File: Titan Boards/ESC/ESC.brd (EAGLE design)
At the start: 101.6 x 101.6 mm, 113 parts, among them Q1 2N2222, Q10 BSS138, Q3 BSS138, Q4 BSS138, Q5 BSS138, Q6 BSS138, Q7 BSS138, Q8 BSS138, Q9 BSS138

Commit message: ESC work
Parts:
- moved CS_7 83.5 mm to (33.3, 21.1)
- moved C7 83.5 mm to (29.7, 21.1)
- moved D9 83.5 mm to (26.9, 24.6)
- moved FUSE_7 83.5 mm to (30.2, 27.9)
- moved Q9 83.5 mm to (20.8, 25.7)
- moved R20 83.5 mm to (27.4, 22.4)
- moved R21 83.5 mm to (23.6, 29.0)
- moved R22 83.5 mm to (23.6, 25.7)
- moved C3 81.5 mm to (65.8, 21.1)
- moved CS_5 81.5 mm to (69.3, 21.1)
- moved D7 81.5 mm to (63.0, 24.6)
- moved FUSE_5 81.5 mm to (66.3, 27.9)
- moved Q7 81.5 mm to (57.1, 25.7)
- moved R14 81.5 mm to (63.5, 22.4)
- moved R15 81.5 mm to (59.7, 29.0)
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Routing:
- net FAULT_8: track 6.49 -> 92.2 mm
- net ANALOG_8: track 0.00 -> 73.9 mm, vias 0 -> 1
- net ANALOG_7: track 0.00 -> 54.1 mm, vias 0 -> 1
- net ANALOG_6: track 0.00 -> 34.6 mm, vias 0 -> 1
- net FUSE_2_TRIGGER: track 4.69 -> 28.7 mm, vias 0 -> 1
- net FUSE_1_TRIGGER: track 5.05 -> 28.6 mm, vias 0 -> 1
- net FUSE_3_TRIGGER: track 4.43 -> 27.6 mm, vias 0 -> 1
- net FUSE_4_TRIGGER: track 4.99 -> 28.2 mm, vias 0 -> 1
- net FUSE_8_TRIGGER: track 4.19 -> 14.0 mm
- net FUSE_6_TRIGGER: track 4.19 -> 14.0 mm
- net FUSE_5_TRIGGER: track 4.19 -> 13.6 mm
- net FUSE_7_TRIGGER: track 4.42 -> 13.8 mm
- net ANALOG_5: track 0.00 -> 6.45 mm, vias 0 -> 1
- net FAULT_7: track 6.74 -> 2.32 mm

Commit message: more esc work
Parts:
- moved Q1 94.1 mm to (4.78, 50.0)
- moved D2 94.1 mm to (9.35, 50.5)
- moved R28 94.1 mm to (9.60, 48.7)
- moved R37 94.1 mm to (9.60, 52.3)
- moved R29 86.7 mm to (2.48, 45.6), turned to 0 degrees
- moved R33 86.7 mm to (2.48, 45.6), turned to 180 degrees
- moved R32 74.7 mm to (2.48, 43.3), turned to 180 degrees
- moved R34 74.7 mm to (2.48, 43.3), turned to 0 degrees
- moved R31 65.5 mm to (2.48, 40.9), turned to 180 degrees
- moved R35 65.5 mm to (2.48, 40.9), turned to 0 degrees
- moved R30 60.4 mm to (2.48, 38.5), turned to 180 degrees
- moved R36 60.4 mm to (2.48, 38.5), turned to 0 degrees
- moved 3-PIN_5 2.10 mm to (66.0, 79.9)
- moved 3-PIN_6 2.10 mm to (48.3, 79.9)
- moved 3-PIN_7 2.10 mm to (30.5, 79.9)
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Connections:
- removed net N$1 (its old number): 24-PIN_CONNECTOR.7,WHITE, 3-PIN_1.WHITE
- removed net N$13: 24-PIN_CONNECTOR.8,WHITE, 3-PIN_5.WHITE
- removed net N$14: 24-PIN_CONNECTOR.8,GREEN, 3-PIN_5.GREEN
- removed net N$15: 24-PIN_CONNECTOR.8,BLUE, 3-PIN_5.BLUE
- removed net N$16: 24-PIN_CONNECTOR.6,WHITE, 3-PIN_6.WHITE
- removed net N$17: 24-PIN_CONNECTOR.6,GREEN, 3-PIN_6.GREEN
- removed net N$18: 24-PIN_CONNECTOR.6,BLUE, 3-PIN_6.BLUE
- removed net N$19: 24-PIN_CONNECTOR.4,WHITE, 3-PIN_7.WHITE
- removed net N$2 (its old number): 24-PIN_CONNECTOR.7,GREEN, 3-PIN_1.GREEN
- removed net N$20: 24-PIN_CONNECTOR.4,BLUE, 3-PIN_7.BLUE
- removed net N$21: 24-PIN_CONNECTOR.4,GREEN, 3-PIN_7.GREEN
- removed net N$22: 24-PIN_CONNECTOR.2,BLUE, 3-PIN_8.BLUE
- removed net N$23: 24-PIN_CONNECTOR.2,GREEN, 3-PIN_8.GREEN
- removed net N$24: 24-PIN_CONNECTOR.2,WHITE, 3-PIN_8.WHITE
- removed net N$3 (its old number): 24-PIN_CONNECTOR.7,BLUE, 3-PIN_1.BLUE
- removed net N$4 (its old number): 24-PIN_CONNECTOR.5,WHITE, 3-PIN_2.WHITE
- removed net N$5 (its old number): 24-PIN_CONNECTOR.5,GREEN, 3-PIN_2.GREEN
- removed net N$6 (its old number): 24-PIN_CONNECTOR.5,BLUE, 3-PIN_2.BLUE
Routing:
- net N$1: track 0.00 -> 146.1 mm
- net N$40: track 133.4 -> 2.11 mm
- net N$2: track 0.00 -> 130.5 mm
- net PWM_4: track 0.00 -> 127.1 mm
- net PWM_8: track 0.00 -> 121.1 mm, vias 0 -> 2
- net N$6: track 0.00 -> 119.4 mm
- net N$3: track 0.00 -> 114.6 mm
- net PWM_3: track 0.00 -> 110.9 mm
- net N$5: track 0.00 -> 105.0 mm
- net PWM_7: track 0.00 -> 104.3 mm, vias 0 -> 2
- net PWM_2: track 0.00 -> 92.4 mm
- net N$4: track 0.00 -> 89.8 mm
- net PWM_6: track 0.00 -> 86.0 mm, vias 0 -> 2
- net FAULT_1: track 7.46 -> 93.4 mm
- net FAULT_8: track 92.2 -> 6.49 mm
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
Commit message: Titan ESC updates
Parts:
- moved Q1 18.6 mm to (-7.02, 35.6)
- moved D2 18.6 mm to (-2.45, 36.1)
- moved R28 18.6 mm to (-2.20, 34.3)
- moved R37 18.6 mm to (-2.20, 37.9)
- moved R36 7.75 mm to (-5.12, 40.0)
- moved R30 7.73 mm to (-5.12, 39.9)
- moved R29 7.73 mm to (-5.12, 47.0)
- moved R31 7.73 mm to (-5.12, 42.3)
- moved R32 7.73 mm to (-5.12, 44.7)
- moved R33 7.73 mm to (-5.12, 47.0)
- moved R35 7.71 mm to (-5.12, 42.2)
- moved R34 7.68 mm to (-5.12, 44.4)
- moved THRUSTER_PWM_1 6.40 mm to (76.0, 38.0)
- moved THRUSTER_PWM_2 6.40 mm to (58.2, 38.0)
- moved THRUSTER_PWM_3 6.40 mm to (40.4, 38.0)
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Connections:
- new net N$10: 24-PIN_CONNECTOR.7,BLUE, 3-PIN_1.BLUE
- new net N$11: 24-PIN_CONNECTOR.7,GREEN, 3-PIN_1.GREEN
- new net N$12: 24-PIN_CONNECTOR.7,WHITE, 3-PIN_1.WHITE
- new net N$13: 24-PIN_CONNECTOR.8,BLUE, 3-PIN_5.WHITE
- new net N$14: 24-PIN_CONNECTOR.8,GREEN, 3-PIN_5.GREEN
- new net N$15: 24-PIN_CONNECTOR.8,WHITE, 3-PIN_5.BLUE
- new net N$16: 24-PIN_CONNECTOR.6,WHITE, 3-PIN_6.WHITE
- new net N$17: 24-PIN_CONNECTOR.6,GREEN, 3-PIN_6.GREEN
- new net N$18: 24-PIN_CONNECTOR.6,BLUE, 3-PIN_6.BLUE
- new net N$19: 24-PIN_CONNECTOR.4,BLUE, 3-PIN_7.BLUE
- new net N$20: 24-PIN_CONNECTOR.4,GREEN, 3-PIN_7.GREEN
- new net N$21: 24-PIN_CONNECTOR.4,WHITE, 3-PIN_7.WHITE
- new net N$22: 24-PIN_CONNECTOR.2,BLUE, 3-PIN_8.BLUE
- new net N$23: 24-PIN_CONNECTOR.2,GREEN, 3-PIN_8.GREEN
- new net N$24: 24-PIN_CONNECTOR.2,WHITE, 3-PIN_8.WHITE
- new net N$7: 24-PIN_CONNECTOR.5,BLUE, 3-PIN_2.BLUE
- new net N$8: 24-PIN_CONNECTOR.5,GREEN, 3-PIN_2.GREEN
- new net N$9: 24-PIN_CONNECTOR.5,WHITE, 3-PIN_2.WHITE
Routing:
- net N$24: track 0.00 -> 85.9 mm
- net N$7: track 0.00 -> 82.7 mm
- net N$5: track 105.0 -> 186.9 mm
- net N$23: track 0.00 -> 79.6 mm
- net N$22: track 0.00 -> 73.2 mm
- net N$8: track 0.00 -> 69.7 mm
- net N$21: track 0.00 -> 65.3 mm
- net N$20: track 0.00 -> 59.0 mm
- net N$9: track 0.00 -> 58.7 mm
- net N$19: track 0.00 -> 52.7 mm
- net N$16: track 0.00 -> 45.2 mm
- net N$10: track 0.00 -> 45.0 mm
- net N$6: track 119.4 -> 162.0 mm
- net N$1: track 146.1 -> 107.0 mm
- net N$17: track 0.00 -> 38.9 mm
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
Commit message: more changes to ESC board
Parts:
- removed Q10, Q9: BSS138, SparkFun-DiscreteSemi:SOT23-3
- removed R29, R30, R31, R32, R33, R34, R35, R36: 2k, rcl:R0603
- removed R37: 4.7K, rcl:R0603
- added IC1: 7425D, 74xx-us:SO14
- added IC2: 74AHC1G08DBV, 74xx-little-us:SOT23-5
- added Q2: 5.8A/30V/35mΩ, SparkFun-DiscreteSemi:SOT23-3
- D10, D3, D4, D5, D6, D7, D8, D9: value RED -> Red
- Q1: value 2N2222 -> 5.8A/30V/35mΩ
- Q3, Q4, Q5, Q6, Q7, Q8: value BSS138 -> 5.8A/30V/35mΩ
- R10, R13, R16, R4, R7: value 190 -> (none)
- R11, R14, R17, R2, R20, R23, R5, R8: value 128 -> (none)
- R12, R15, R18, R6, R9: value 2.2K -> 28
- R19, R22, R25: value 190 -> 28
- R21, R24, R3: value 2.2K -> (none)
- moved D2 116.7 mm to (99.0, 93.8), turned to 135 degrees
- moved Q1 85.3 mm to (76.2, 16.9)
- moved R13 60.4 mm to (79.5, 17.7), flipped to the bottom, turned to 180 degrees
- moved Q4 41.3 mm to (16.2, 16.7)
- moved Q3 39.7 mm to (36.4, 16.8)
- moved R18 38.8 mm to (79.5, 16.4), flipped to the top, turned to 180 degrees
- moved Q5 36.9 mm to (76.2, 16.9), flipped to the bottom
- moved Q6 34.9 mm to (56.4, 16.7), flipped to the bottom
- moved R10 24.2 mm to (12.7, 17.8), turned to 180 degrees
- moved Q8 22.6 mm to (16.2, 16.7)
- moved CS_1 22.5 mm to (84.5, 21.1)
- moved R7 22.2 mm to (32.8, 17.5), turned to 180 degrees
- moved CS_2 20.8 mm to (64.5, 21.2)
- moved R4 20.7 mm to (52.8, 17.8), turned to 180 degrees
- moved Q7 20.7 mm to (36.4, 16.8)
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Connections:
- removed net N$54: D10.A, R23.1
- removed net N$59: D2.C, R28.1
- new net N$32: D3.C, Q1.3
- new net NOR_1_OUT: IC1.6, IC2.1
- new net NOR_2_OUT: IC1.8, IC2.2
- net +5V: now also IC1.11, IC1.14, IC1.3, IC2.5, R12.2, R15.2, R18.2, R19.2, R22.2, R25.2, R6.2, R9.2; no longer Q1.3, R11.2, R14.2, R17.2, R2.2, R20.2, R23.2, R5.2, R8.2
- net FAULT_1: now also IC1.1, Q1.1, R2.1, R3.2; no longer D3.C, Q3.3, R33.1
- net FAULT_2: now also IC1.2, Q2.1, R4.1, R5.2; no longer D4.C, Q4.3, R32.1
- net FAULT_3: now also IC1.4, Q3.1, R7.1, R8.2; no longer D5.C, Q5.3, R31.1
- net FAULT_4: now also IC1.5, Q4.1, R10.1, R11.2; no longer D6.C, Q6.3, R30.1
- net FAULT_5: now also IC1.9, Q5.1, R13.1, R14.2; no longer D7.C, Q7.3, R29.1
- net FAULT_6: now also IC1.10, Q6.1, R16.1, R17.2; no longer D8.C, Q8.3, R34.1
- net FAULT_7: now also IC1.12, Q7.1, R20.1, R21.2; no longer D9.C, Q9.3, R35.1
- net FAULT_8: now also IC1.13, Q8.1, R23.1, R24.2; no longer D10.C, Q10.3, R36.1
- net FUSE_1_TRIGGER: now also R2.2; no longer R3.2
- net FUSE_2_TRIGGER: now also R4.2; no longer R6.2
- net FUSE_3_TRIGGER: now also R7.2; no longer R9.2
- net FUSE_4_TRIGGER: now also R10.2; no longer R12.2
- net FUSE_5_TRIGGER: now also R13.2; no longer R15.2
- net FUSE_6_TRIGGER: now also R16.2; no longer R18.2
- net FUSE_7_TRIGGER: now also R20.2; no longer R21.2
- net FUSE_8_TRIGGER: now also R23.2; no longer R24.2
- net GND: now also D2.C, IC1.7, IC2.3, Q1.2, Q2.2, R11.1, R14.1, R17.1, R21.1, R24.1, R3.1, R5.1, R8.1; no longer Q10.2, Q9.2, R10.1, R13.1, R16.1, R19.1, R22.1, R25.1, R28.2, R37.2, R4.1, R7.1
- net N$13: now also 24-PIN_CONNECTOR.8,WHITE; no longer 24-PIN_CONNECTOR.8,BLUE
- net N$15: now also 24-PIN_CONNECTOR.8,BLUE; no longer 24-PIN_CONNECTOR.8,WHITE
- net N$31: now also IC2.4, R28.2; no longer D3.A, R2.1
- net N$33: now also D3.A, R18.1; no longer D4.A, R5.1
- net N$34: now also D4.C, Q2.3; no longer Q3.1, R3.1, R4.2
- net N$36: now also D4.A; no longer Q4.1, R7.2
- net N$37: now also D5.C, Q3.3; no longer D5.A, R8.1
- net N$40: now also D5.A, R9.1; no longer Q1.1, R29.2, R30.2, R31.2, R32.2, R33.2, R34.2, R35.2, R36.2
- net N$41: now also D6.C, Q4.3; no longer Q5.1, R10.2, R9.1
- net N$42: now also R12.1; no longer R11.1
- net N$44: now also D7.C, Q5.3; no longer Q6.1, R12.1, R13.2
- net N$45: now also R15.1; no longer R14.1
- net N$46: now also D8.C, Q6.3; no longer D2.A, Q1.2, R37.1
- net N$47: now also D8.A, R19.1; no longer Q7.1, R15.1, R16.2
- net N$48: now also D9.C, Q7.3; no longer D8.A, R17.1
- net N$50: now also D9.A, R22.1; no longer Q8.1, R18.1, R19.2
- net N$51: now also D10.C, Q8.3; no longer D9.A, R20.1
- net N$53: now also D10.A, R25.1; no longer Q9.1, R21.1, R22.2
- net N$56: now also D2.A, R28.1; no longer Q10.1, R24.1, R25.2
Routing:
- net N$56: track 3.18 -> 137.9 mm
- net N$4: track 94.5 -> 191.9 mm
- net FAULT_1: track 93.4 -> 2.91 mm
- net FAULT_2: track 73.0 -> 3.05 mm
- net FAULT_5: track 68.0 -> 2.77 mm, vias 2 -> 0
- net +5V: track 53.9 -> 0.00 mm
- net FAULT_3: track 53.6 -> 3.16 mm
- net FAULT_6: track 49.1 -> 2.89 mm, vias 2 -> 0
- net PWM_5: track 45.1 -> 80.6 mm
- net FAULT_4: track 32.4 -> 3.10 mm, vias 2 -> 0
- net FAULT_7: track 29.1 -> 3.12 mm, vias 2 -> 0
- net PWM_8: track 114.3 -> 137.9 mm
- net PWM_7: track 96.8 -> 118.6 mm, vias 0 -> 2
- net ANALOG_8: track 71.9 -> 92.4 mm
- net PWM_6: track 79.9 -> 99.8 mm
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- removed copper zone on layer 1, net +3V3
- removed copper zone on layer 16, net +3V3
- removed copper zone on layer 1, net +5V
- removed copper zone on layer 16, net +5V
- removed copper zone on layer 16, net GND
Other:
- outline, holes or cut-outs redrawn

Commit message: ESC board updates
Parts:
- removed THRUSTER_PWM_1: 1, pinhead:1X03
- removed THRUSTER_PWM_2, THRUSTER_PWM_3, THRUSTER_PWM_4, THRUSTER_PWM_5, THRUSTER_PWM_6, THRUSTER_PWM_7, THRUSTER_PWM_8: (no value), pinhead:1X03
- added U$1, U$2, U$3, U$4, U$5, U$6, U$7, U$8: MALE1PINHEADER, Male_Header_1Pin:MALE1PINHEADER
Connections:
- net GND: no longer THRUSTER_PWM_1.3, THRUSTER_PWM_2.3, THRUSTER_PWM_3.3, THRUSTER_PWM_4.3, THRUSTER_PWM_5.3, THRUSTER_PWM_6.3, THRUSTER_PWM_7.3, THRUSTER_PWM_8.3
- net PWM_1: now also U$1.PWM; no longer THRUSTER_PWM_1.1
- net PWM_2: now also U$2.PWM; no longer THRUSTER_PWM_2.1
- net PWM_3: now also U$3.PWM; no longer THRUSTER_PWM_3.1
- net PWM_4: now also U$4.PWM; no longer THRUSTER_PWM_4.1
- net PWM_5: now also U$5.PWM; no longer THRUSTER_PWM_5.1
- net PWM_6: now also U$6.PWM; no longer THRUSTER_PWM_6.1
- net PWM_7: now also U$7.PWM; no longer THRUSTER_PWM_7.1
- net PWM_8: now also U$8.PWM; no longer THRUSTER_PWM_8.1
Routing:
- net PWM_8: track 137.9 -> 13.4 mm
- net PWM_4: track 125.4 -> 14.1 mm
- net FAULT_5: track 2.77 -> 111.6 mm, vias 0 -> 3
- net FAULT_1: track 2.91 -> 110.0 mm, vias 0 -> 2
- net PWM_7: track 118.6 -> 13.4 mm, vias 2 -> 0
- net PWM_3: track 107.0 -> 14.3 mm
- net FAULT_6: track 2.89 -> 90.8 mm, vias 0 -> 3
- net PWM_6: track 99.8 -> 13.6 mm, vias 2 -> 0
- net FAULT_2: track 3.05 -> 88.1 mm, vias 0 -> 2
- net PWM_2: track 88.5 -> 14.3 mm
- net FAULT_7: track 3.12 -> 72.1 mm, vias 0 -> 3
- net PWM_5: track 80.6 -> 13.8 mm, vias 2 -> 0
- net FAULT_3: track 3.16 -> 61.7 mm, vias 0 -> 4
- net FAULT_8: track 3.31 -> 48.7 mm, vias 0 -> 1
- net FAULT_4: track 3.10 -> 40.0 mm
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- added copper zone on layer 16, net GND

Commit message: FInal ESC after review
See summary
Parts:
- moved 3-PIN_6 0.15 mm to (56.3, 86.5)
- moved 3-PIN_7 0.15 mm to (36.3, 86.5)
- moved 3-PIN_5 0.11 mm to (76.1, 86.5)
- moved C10 0.07 mm to (89.3, 12.7)
- renumbered FUSE_1 to F1, FUSE_2 to F2, FUSE_3 to F3, FUSE_4 to F4, FUSE_5 to F5, FUSE_6 to F6, FUSE_7 to F7, FUSE_8 to F8
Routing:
- net +5V: track 0.00 -> 222.5 mm, vias 0 -> 24
- net +3V3: track 3.71 -> 97.0 mm, vias 0 -> 4
- net GND: track 5.34 -> 92.4 mm, vias 14 -> 37
- net NOR_1_OUT: track 17.2 -> 20.2 mm
- added copper zone on layer 1, net +3V3
- added copper zone on layer 16, net +3V3
- added copper zone on layer 1, net +5V
- added copper zone on layer 16, net +5V

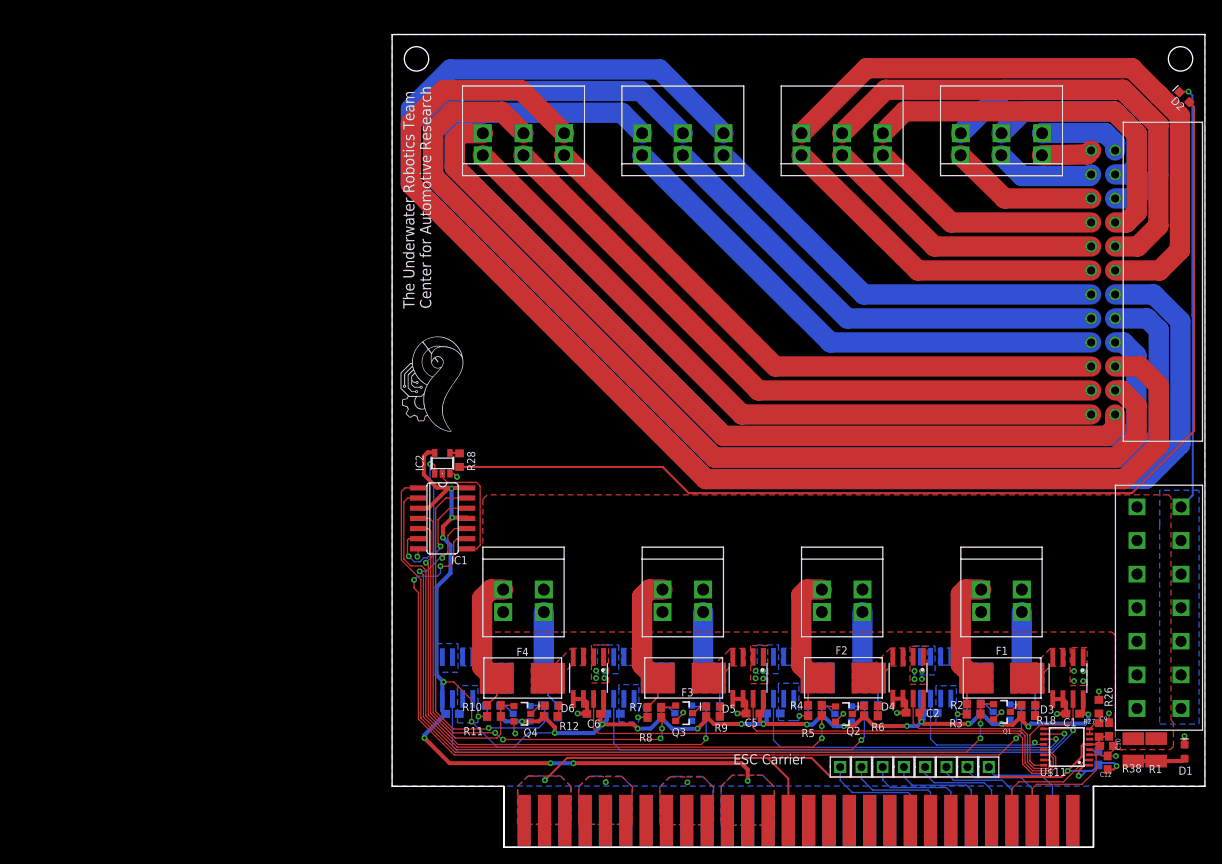
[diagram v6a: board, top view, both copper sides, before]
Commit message: final commit of Titan ESC
slight cosmetic changes to ESC board
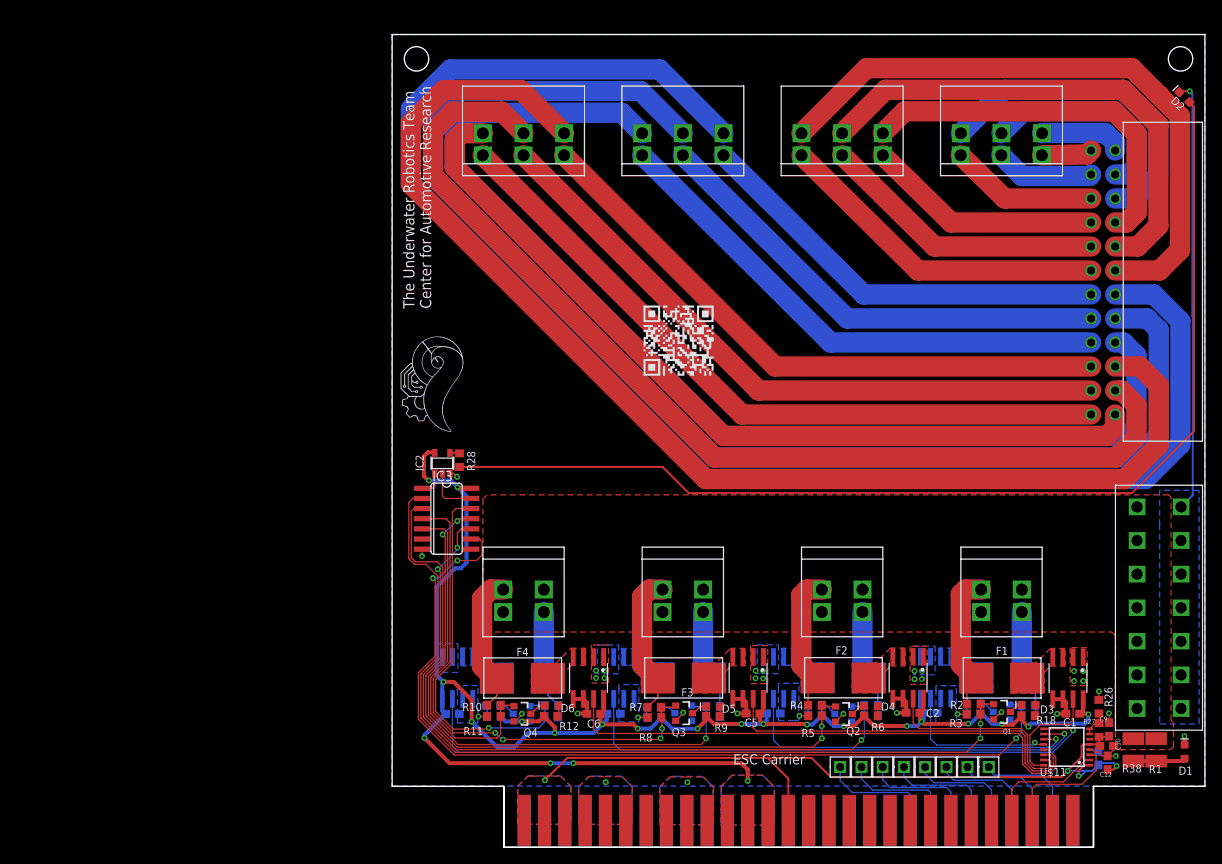
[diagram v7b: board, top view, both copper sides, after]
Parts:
- removed IC1: 7425D, 74xx-us:SO14
- added IC3: 4002D, 40xx:SO14
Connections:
- net +5V: now also IC3.14; no longer IC1.11, IC1.14, IC1.3
- net FAULT_1: now also IC3.2; no longer IC1.1
- net FAULT_2: now also IC3.3; no longer IC1.2
- net FAULT_3: now also IC3.4; no longer IC1.4
- net FAULT_4: now also IC3.5; no longer IC1.5
- net FAULT_5: now also IC3.9; no longer IC1.9
- net FAULT_6: now also IC3.10; no longer IC1.10
- net FAULT_7: now also IC3.11; no longer IC1.12
- net FAULT_8: now also IC3.12; no longer IC1.13
- net GND: now also IC3.7; no longer IC1.7
- net NOR_1_OUT: now also IC3.1; no longer IC1.6
- net NOR_2_OUT: now also IC3.13; no longer IC1.8
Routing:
- net NOR_1_OUT: track 20.2 -> 3.23 mm, vias 2 -> 0
- net NOR_2_OUT: track 14.8 -> 6.53 mm
- net +5V: track 222.5 -> 217.1 mm, vias 24 -> 23
- net FAULT_3: track 61.7 -> 64.1 mm
- net FAULT_4: track 40.0 -> 42.4 mm
- net FAULT_7: track 72.1 -> 70.4 mm
- net FAULT_8: track 48.7 -> 47.2 mm
- net FAULT_6: track 90.8 -> 90.0 mm
- net FAULT_5: track 111.6 -> 112.4 mm
- net FAULT_2: track 88.1 -> 88.6 mm

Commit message: ESC Updates + library additions
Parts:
- 2-PIN_1, 2-PIN_2, 2-PIN_3, 2-PIN_4, 2-PIN_5, 2-PIN_6, 2-PIN_7, 2-PIN_8: value 1711725 -> 1755736; device Screw_Terminals:1711725 -> Screw_Terminals:1755736
- 3-PIN_1, 3-PIN_2, 3-PIN_3, 3-PIN_4, 3-PIN_5, 3-PIN_6, 3-PIN_7, 3-PIN_8: value 1711738 -> 1755749; device Screw_Terminals:1711738 -> Screw_Terminals:1755749
- R12, R15, R18, R19, R22, R25, R6, R9: value 28 -> 150
- R28: value 15 -> 91
- moved IC2 5.92 mm to (5.67, 53.9)
- moved R28 5.92 mm to (7.82, 54.3)
- moved IC3 5.92 mm to (6.20, 47.0)
- moved 2-PIN_1 4.50 mm to (76.2, 36.7)
- moved 2-PIN_2 4.50 mm to (56.3, 36.7)
- moved 2-PIN_3 4.50 mm to (36.3, 36.7)
- moved 2-PIN_4 4.50 mm to (16.4, 36.7)
- moved 3-PIN_8 4.46 mm to (16.4, 82.0), turned to 180 degrees
- moved 3-PIN_6 4.46 mm to (56.3, 82.0), turned to 180 degrees
- moved 3-PIN_7 4.46 mm to (36.3, 82.0), turned to 180 degrees
- moved 3-PIN_5 4.43 mm to (76.2, 82.1), turned to 179.8 degrees
- turned 3-PIN_1 to 180 degrees
- turned 3-PIN_2 to 180 degrees
- turned 3-PIN_3 to 180 degrees
- turned 3-PIN_4 to 180 degrees
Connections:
- removed net N$1 (its old number): 24-PIN_CONNECTOR.1,BLUE, 3-PIN_4.BLUE
- removed net N$10: 24-PIN_CONNECTOR.7,BLUE, 3-PIN_1.BLUE
- removed net N$12: 24-PIN_CONNECTOR.7,WHITE, 3-PIN_1.WHITE
- removed net N$2 (its old number): 24-PIN_CONNECTOR.1,GREEN, 3-PIN_4.GREEN
- removed net N$3 (its old number): 24-PIN_CONNECTOR.1,WHITE, 3-PIN_4.WHITE
- removed net N$4 (its old number): 24-PIN_CONNECTOR.3,WHITE, 3-PIN_3.WHITE
- removed net N$7 (its old number): 24-PIN_CONNECTOR.5,BLUE, 3-PIN_2.BLUE
- removed net N$8 (its old number): 24-PIN_CONNECTOR.5,GREEN, 3-PIN_2.GREEN
- removed net N$9 (its old number): 24-PIN_CONNECTOR.5,WHITE, 3-PIN_2.WHITE
- net FUSE_1_TRIGGER: now also 2-PIN_1.P$1; no longer 2-PIN_1.BLACK
- net FUSE_2_TRIGGER: now also 2-PIN_2.P$1; no longer 2-PIN_2.BLACK
- net FUSE_3_TRIGGER: now also 2-PIN_3.P$1; no longer 2-PIN_3.BLACK
- net FUSE_4_TRIGGER: now also 2-PIN_4.P$1; no longer 2-PIN_4.BLACK
- net FUSE_5_TRIGGER: now also 2-PIN_5.P$1; no longer 2-PIN_5.BLACK
- net FUSE_6_TRIGGER: now also 2-PIN_6.P$1; no longer 2-PIN_6.BLACK
- net FUSE_7_TRIGGER: now also 2-PIN_7.P$1; no longer 2-PIN_7.BLACK
- net FUSE_8_TRIGGER: now also 2-PIN_8.P$1; no longer 2-PIN_8.BLACK
- net N$5: now also 24-PIN_CONNECTOR.7,BLUE, 3-PIN_1.WHITE; no longer 24-PIN_CONNECTOR.3,GREEN, 3-PIN_3.GREEN
- net N$6: now also 24-PIN_CONNECTOR.7,WHITE, 3-PIN_1.BLUE; no longer 24-PIN_CONNECTOR.3,BLUE, 3-PIN_3.BLUE
- net VOLTAGE_INPUT: now also 2-PIN_1.P$2, 2-PIN_2.P$2, 2-PIN_3.P$2, 2-PIN_4.P$2, 2-PIN_5.P$2, 2-PIN_6.P$2, 2-PIN_7.P$2, 2-PIN_8.P$2; no longer 2-PIN_1.RED, 2-PIN_2.RED, 2-PIN_3.RED, 2-PIN_4.RED, 2-PIN_5.RED, 2-PIN_6.RED, 2-PIN_7.RED, 2-PIN_8.RED
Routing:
- net N$4 (its old number): track 192.0 -> 0.00 mm
- net N$5: track 167.7 -> 0.00 mm
- net N$3 (its old number): track 155.1 -> 0.00 mm
- net N$6: track 142.2 -> 0.00 mm
- net N$2 (its old number): track 130.0 -> 0.00 mm
- net N$1 (its old number): track 105.8 -> 0.00 mm
- net N$7 (its old number): track 79.0 -> 0.00 mm
- net N$8 (its old number): track 62.7 -> 0.00 mm
- net N$9 (its old number): track 47.1 -> 0.00 mm
- net N$10: track 41.6 -> 0.00 mm
- net N$4: track 26.3 -> 0.00 mm
- net N$12: track 10.6 -> 0.00 mm
- net +5V: track 217.1 -> 223.2 mm
- net FAULT_5: track 112.4 -> 118.2 mm
- net FAULT_6: track 90.0 -> 95.6 mm
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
